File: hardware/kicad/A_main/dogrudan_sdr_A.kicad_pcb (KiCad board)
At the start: 6 copper layers, 235 x 225 mm, 270 parts, among them J1 XT60, J10 JTAG 2x3, J20 SMA A1, J21 SMA B1, J22 SMA A2, J23 SMA B2, J30 SMA TX1, J31 SMA TX2, J32 SMA TX3, J33 SMA TX4, J40 HR911130A, J41 HR911130A, J60 GPS modul, J61 SMA 10MHz ref, J62 DAC modul, J63 C kartina, J64 UART 3.3V, J65 C kartina #2, J66 D kartina, Q1 DMP3098L, SW1 PROG, T1 ADT1-1WT+, T10 ADT1-1WT+, T11 ADT1-1WT+, T12 ADT1-1WT+, T13 ADT1-1WT+, T2 ADT1-1WT+, T3 ADT1-1WT+, T4 ADT1-1WT+, U1 TPS62130, U10 LFE5U-25F-7BG256I, U11 W25Q128JVSIQ, U15 ADCLK846BCPZ, U16 SN65LVDS2DBVR, U17 SN65LVDS2DBVR, U18 SN65LVDS2DBVR, U2 TPS62130, U20 AD9251BCPZ-80, U21 AD9251BCPZ-80, U3 TPS7A2033, U30 AD9767ASTZ, U31 AD9767ASTZ, U4 ADP150, U40 RTL8211FI-CG, U41 RTL8211FI-CG, U5 ADP150, U50 W9825G6KH-6I, U6 ADP150, U62 TLV3501AIDBVR, U7 ADP150, U8 ADP150, U9 ADP150, Y10 ABLNO-V-80.000MHZ, Y610 25MHz, Y626 25MHz

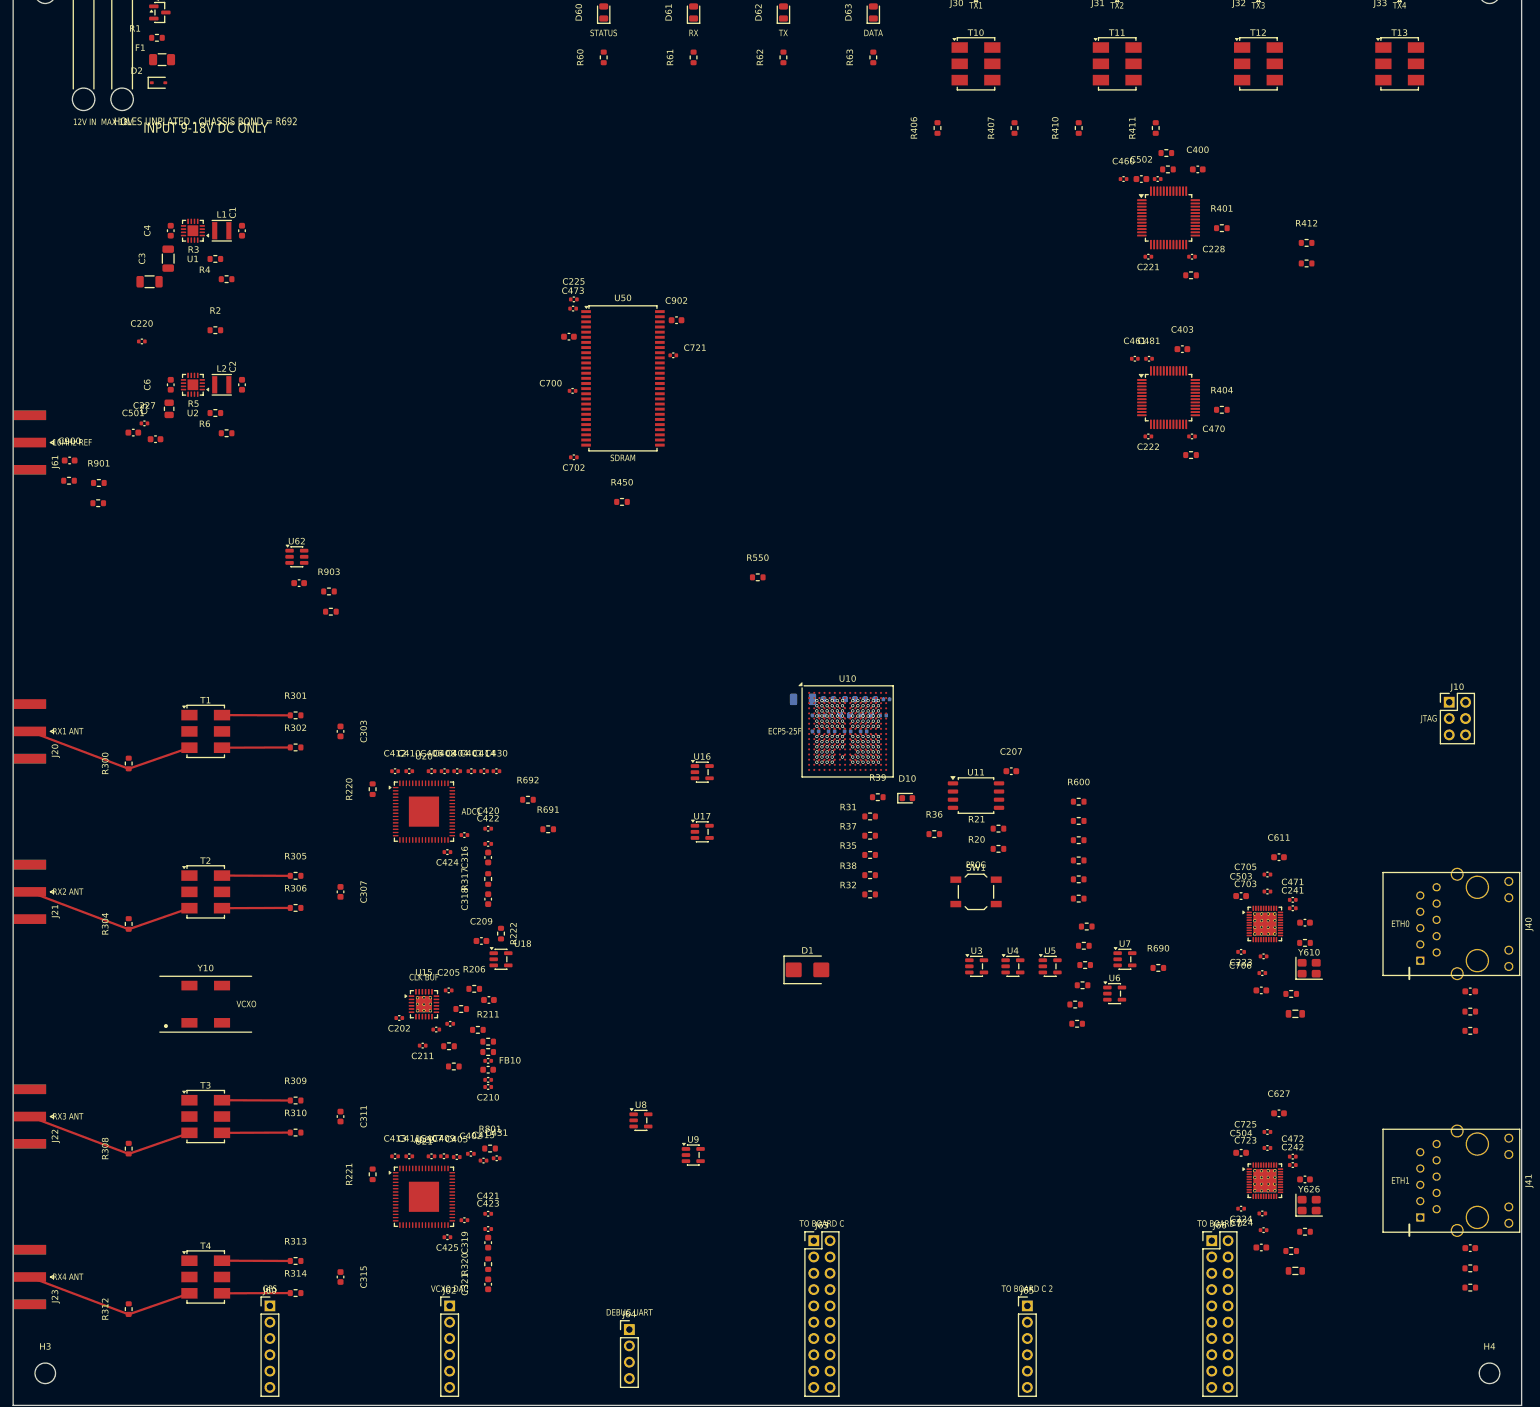
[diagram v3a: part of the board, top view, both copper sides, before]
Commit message: Correct the schematic faults that ERC cannot find
An agent examined the three schematics against the datasheets. ERC
reported zero violations before and after this work. None of these
faults are visible to ERC.

The comparator for the external 10 MHz reference was in shutdown. The
SHDN pin of the TLV3501 went to +3V3. Sixteen DRV8833 devices had VCP
and VINT unconnected. Without the charge pump none of the 28 filter
relays can latch. Seven regulators had no decoupling capacitor within
18 mm to 94 mm. On board D the nearest +12V capacitor to an LM358 was
227 mm away on a 275 mm board.

The PE4312 devices had no series 10k resistor on pin 3. The datasheet
makes this necessary for the attenuation accuracy. Their exposed pad
was 2.6 mm against 2.15 mm. The BOM did not give the load capacitance
of the crystal. This work added 60 parts and changed 4 footprints.

The worst fault was in the tool chain. lib/gen_symbols.py still made
the old pin numbers. The five corrections went into the symbol
library by hand and not into its generator. A new library would have
removed all of them.

The thermal vias are now a decision from the measured clearance and
the dissipation. This work removed them from the PE4312, the RTL8211F
and the ADCLK846. They stay on the DRV8833 and on the LM5164, which
is a 1 W buck converter.

Two checks are new. sema_denetim compares the pin names with the
nets. netlist_denetim locks 22 pin-to-net expectations from the
datasheets and does not need a board.

The boards were built again with these corrections. The chain now
adds the test points: 10 on board A, 7 on board C and 15 on board D.
Each board has 3 fiducials. Every pad has a net.
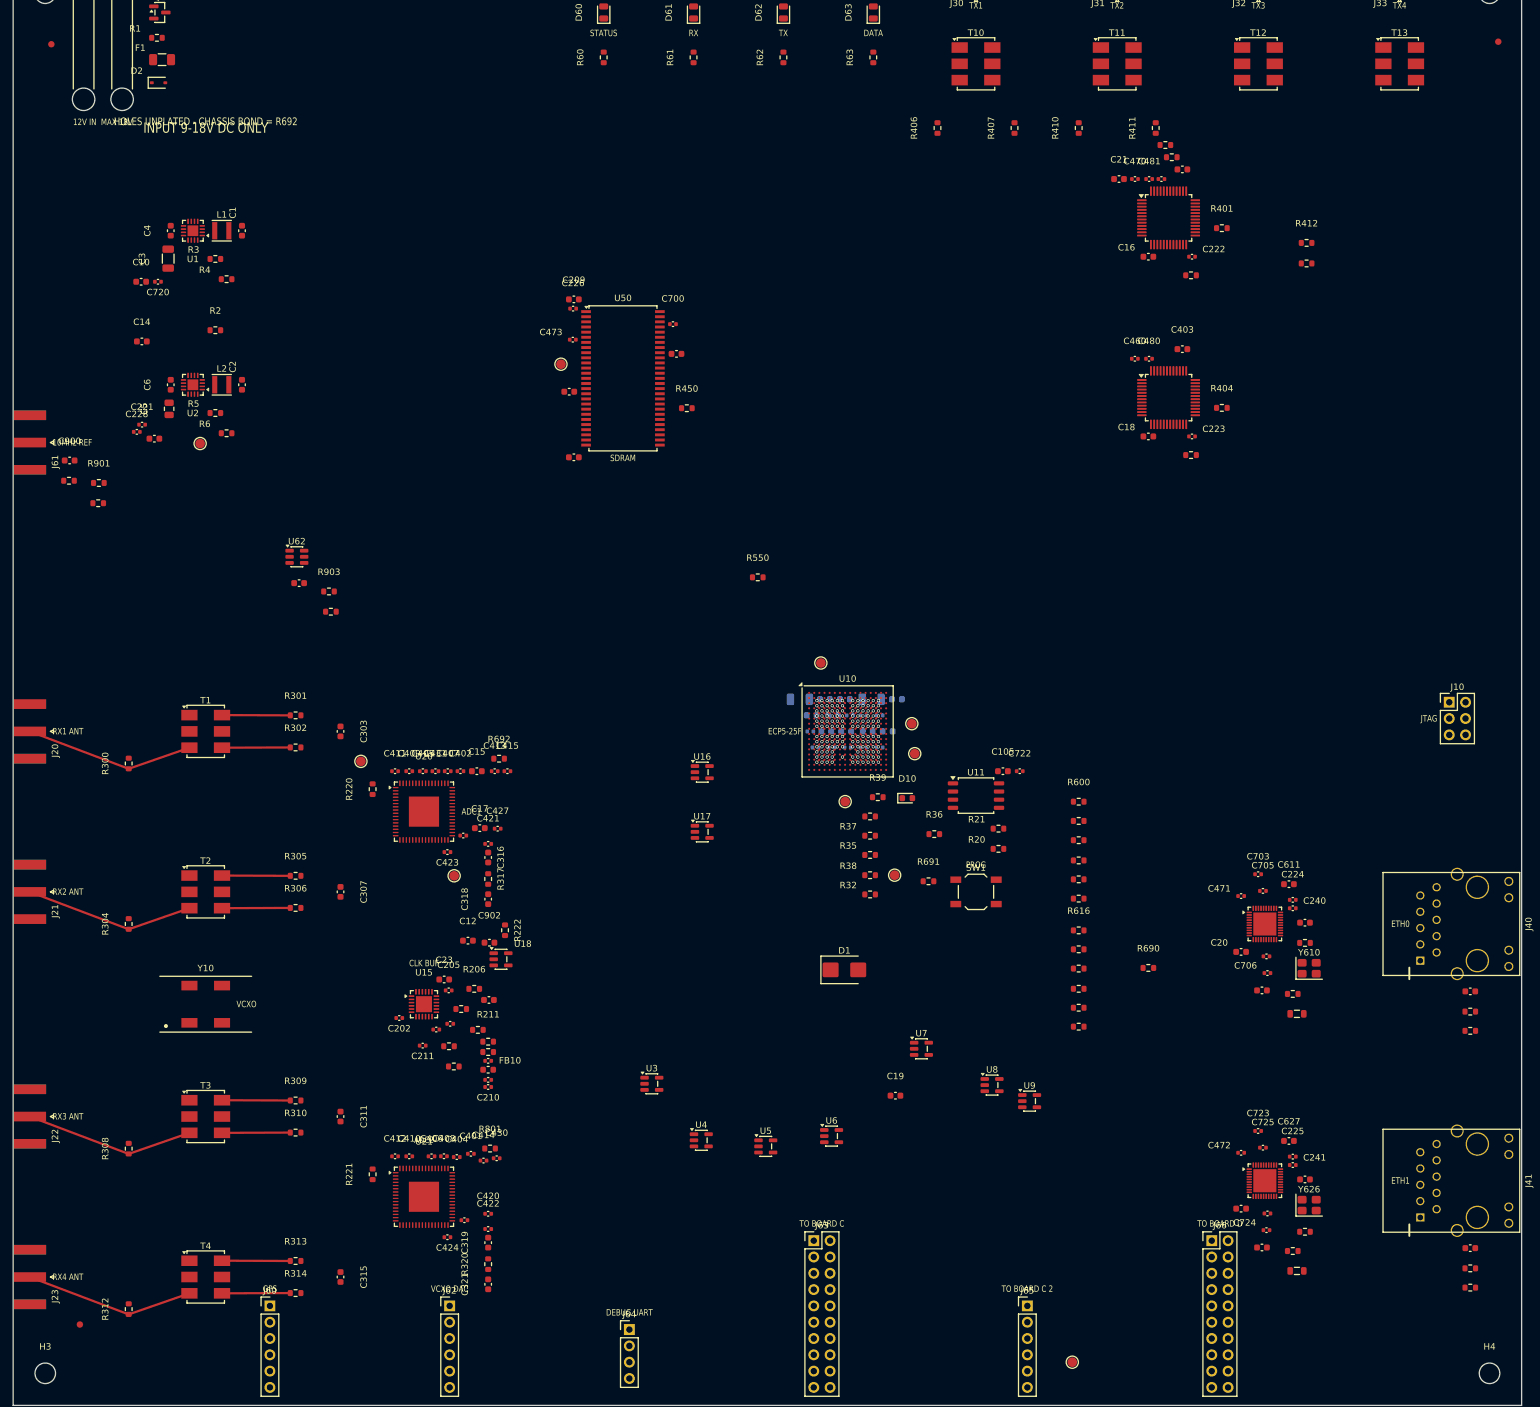
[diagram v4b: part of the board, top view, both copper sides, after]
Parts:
- added C10: 1uF, C_0603_1608Metric, F.Cu at (19.9, 50.0)
- added C11: 1uF, C_0603_1608Metric, B.Cu at (137.7, 115.0)
- added C12: 1uF, C_0603_1608Metric, F.Cu at (70.9, 152.6)
- added C13: 1uF, C_0603_1608Metric, B.Cu at (124.4, 117.5)
- added C14: 1uF, C_0603_1608Metric, F.Cu at (20.1, 59.2)
- added C15: 1uF, C_0603_1608Metric, F.Cu at (72.2, 126.2)
- added C16: 1uF, C_0603_1608Metric, F.Cu at (176.8, 46.0)
- added C17: 1uF, C_0603_1608Metric, F.Cu at (72.7, 135.1)
- added C18: 1uF, C_0603_1608Metric, F.Cu at (176.8, 74.0)
- added C19: 1uF, C_0603_1608Metric, F.Cu at (137.4, 176.8)
- added C20: 1uF, C_0603_1608Metric, F.Cu at (191.3, 154.3)
- added C21: 1uF, C_0603_1608Metric, F.Cu at (172.3, 34.0)
- added C22: 1uF, C_0603_1608Metric, B.Cu at (127.7, 117.5)
- added C23: 1uF, C_0603_1608Metric, F.Cu at (67.2, 158.7)
- added FID1: ​FID, Fiducial_1mm_Mask2mm, F.Cu at (5.95, 12.9)
- added FID2: ​FID, Fiducial_1mm_Mask2mm, F.Cu at (231.4, 12.6)
- added FID3: ​FID, Fiducial_1mm_Mask2mm, F.Cu at (10.4, 212.4)
- added TP1: ​+1V1, TestPoint_Pad_D1.5mm, F.Cu at (29.1, 75.2)
- added TP10: ​REF10_IN, TestPoint_Pad_D1.5mm, F.Cu at (125.8, 109.3)
- added TP2: ​+1V8_A, TestPoint_Pad_D1.5mm, F.Cu at (54.2, 124.7)
- added TP3: ​+1V8_D, TestPoint_Pad_D1.5mm, F.Cu at (68.7, 142.5)
- added TP4: ​+2V5, TestPoint_Pad_D1.5mm, F.Cu at (140.0, 118.8)
- added TP5: ​+3V3, TestPoint_Pad_D1.5mm, F.Cu at (85.3, 62.8)
- added TP6: ​VIN_PROT, TestPoint_Pad_D1.5mm, F.Cu at (165.0, 218.3)
- added TP7: ​FPGA_CLK80, TestPoint_Pad_D1.5mm, F.Cu at (140.5, 123.5)
- added TP8: ​DONE, TestPoint_Pad_D1.5mm, F.Cu at (137.3, 142.4)
- added TP9: ​nINIT, TestPoint_Pad_D1.5mm, F.Cu at (129.6, 130.9)
- C104, C220, C227, C242, C502, C504, C702, C721: moved to B.Cu
- C105, C226, C240, C720, C722: moved to F.Cu
- U15: footprint HVQFN-24-1EP_4x4mm_P0.5mm_EP2.5x2.5mm_ThermalVias -> HVQFN-24-1EP_4x4mm_P0.5mm_EP2.5x2.5mm
- U40, U41: footprint QFN-40-1EP_5x5mm_P0.4mm_EP3.6x3.6mm_ThermalVias -> QFN-40-1EP_5x5mm_P0.4mm_EP3.6x3.6mm
- Y610, Y626: value 25MHz -> 25MHz CL12pF
- moved C225 174.3 mm to (199.3, 186.2)
- moved C228 166.6 mm to (19.3, 73.3)
- moved C221 158.9 mm to (20.1, 72.2)
- moved C104 129.9 mm to (133.7, 115.0)
- moved C720 126.2 mm to (22.6, 50.0)
- moved C220 124.7 mm to (130.4, 117.5)
- moved C503 124.4 mm to (87.3, 77.3)
- moved C227 120.9 mm to (132.5, 117.5)
- moved C902 101.3 mm to (74.2, 152.9)
- moved C209 101.0 mm to (87.3, 52.7)
- moved C502 97.6 mm to (129.8, 120.0)
- moved C242 95.1 mm to (135.0, 117.5)
- moved C504 87.7 mm to (133.1, 120.0)
- moved C223 80.7 mm to (183.7, 74.0)
- moved C240 80.2 mm to (199.3, 147.6)
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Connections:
- U62 pad 6: +3V3 -> GND
